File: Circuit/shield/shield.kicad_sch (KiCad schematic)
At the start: 6 parts, among them J1 Power, J2 Digital/PWM, J3 Analog, J4 Digital/PWM, J5 AE-TB6612, J6 Battery

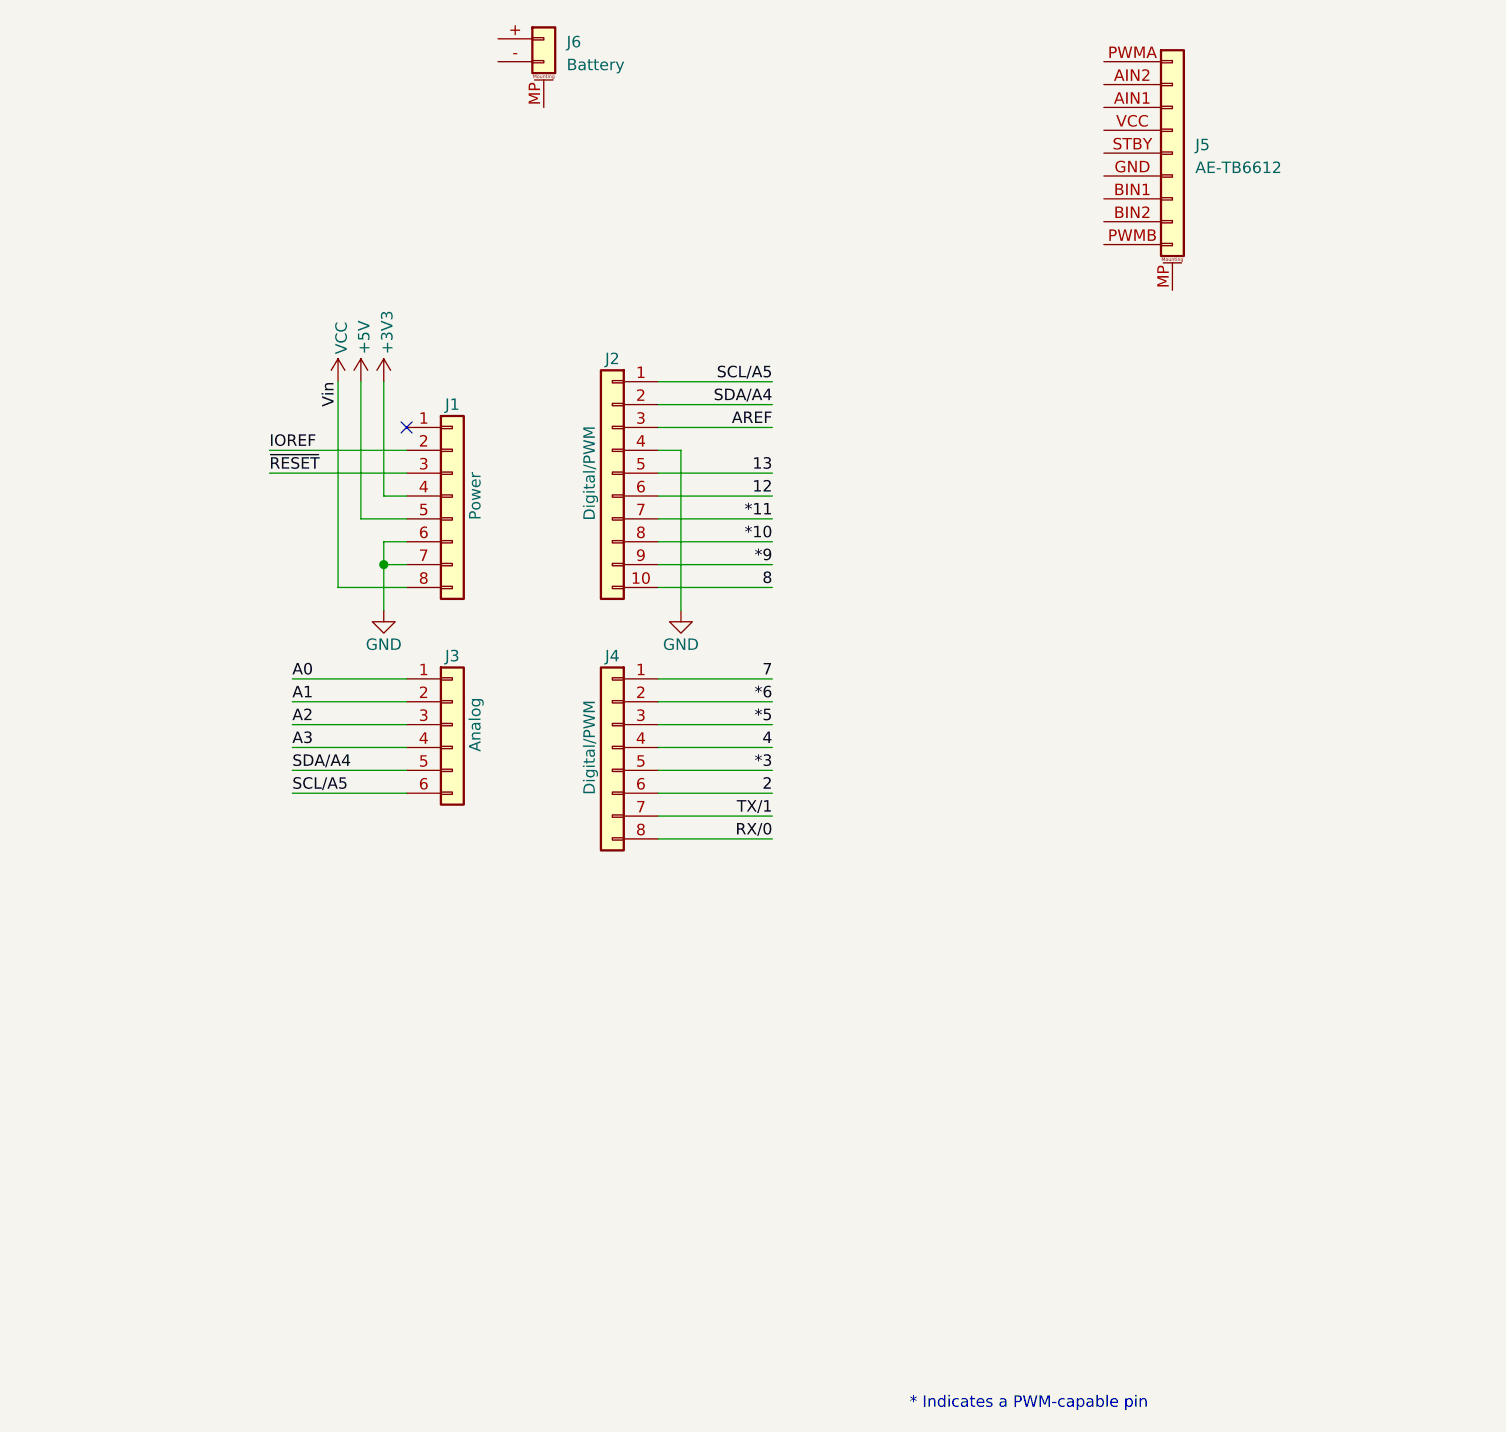
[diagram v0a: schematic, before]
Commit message: Make shield circuit
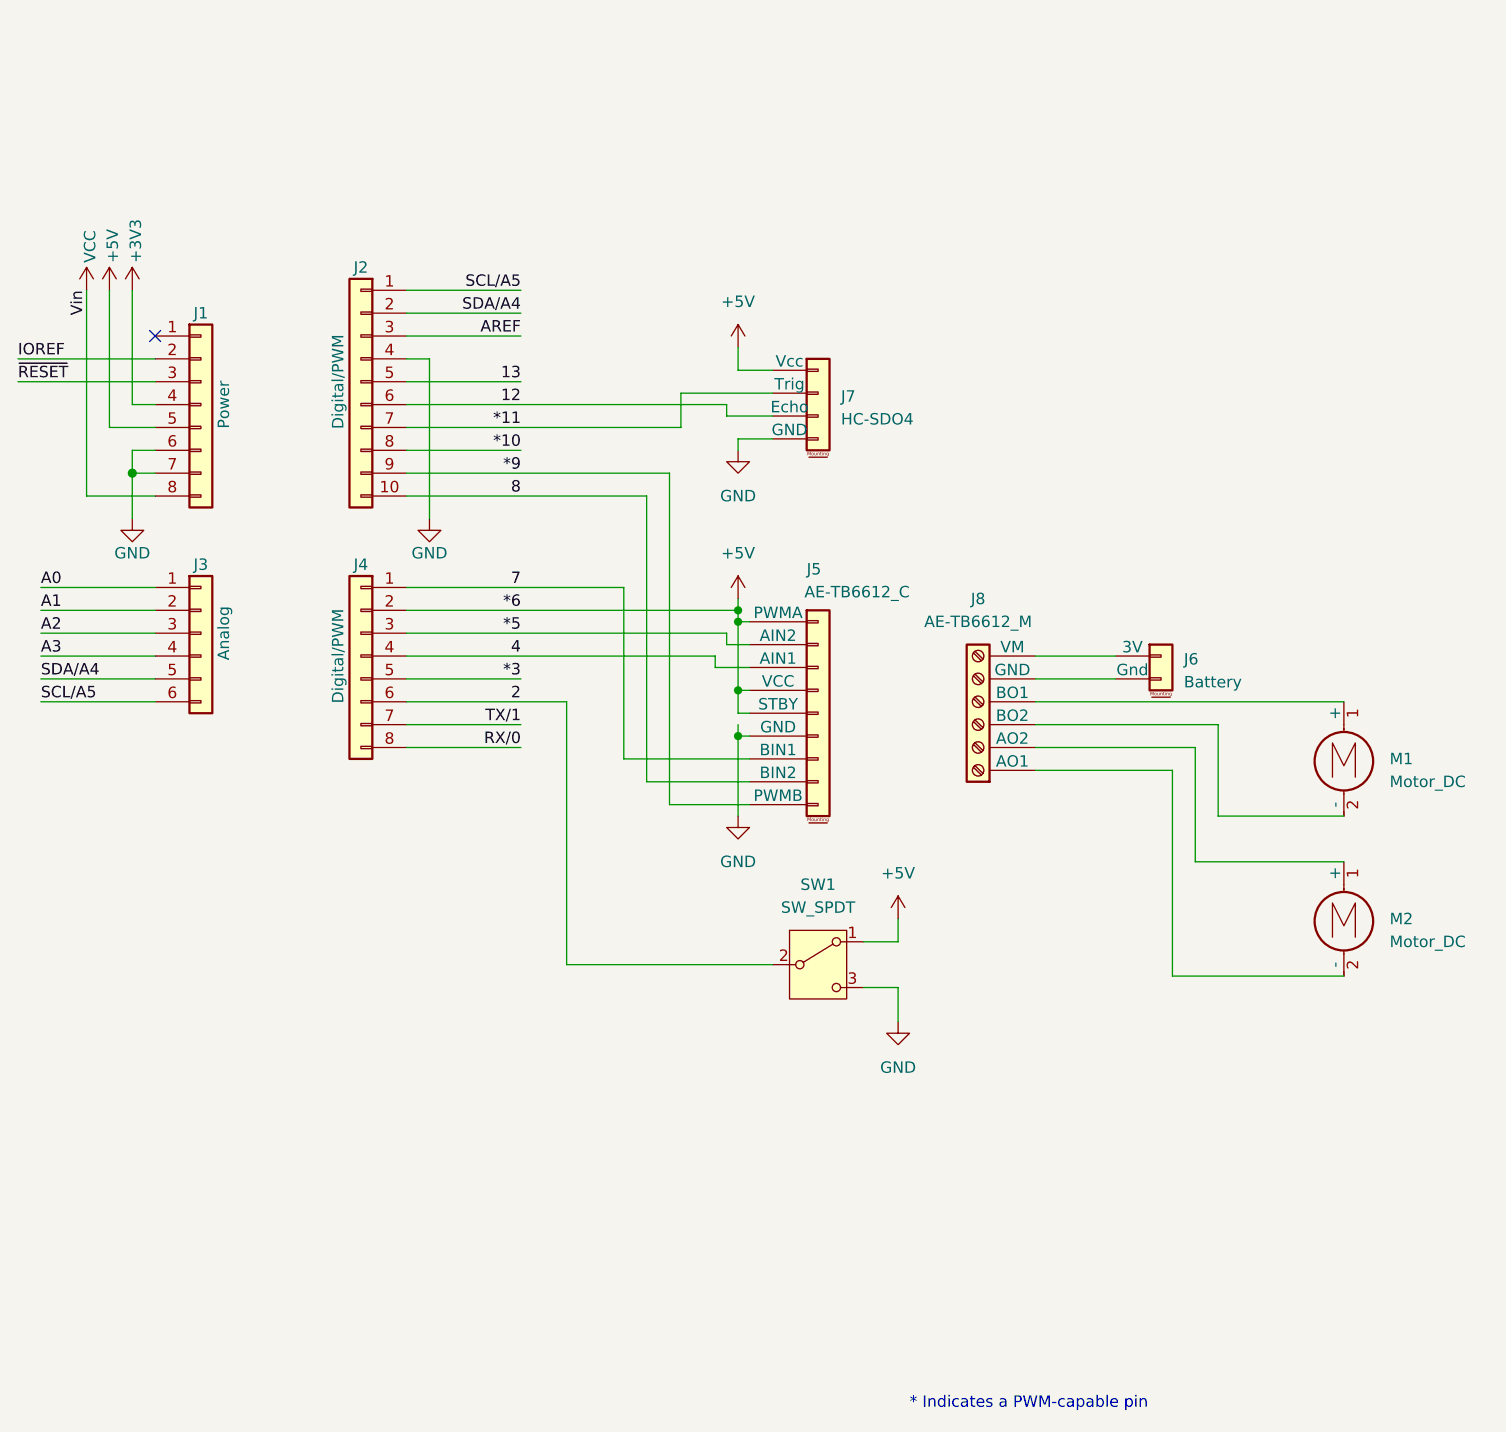
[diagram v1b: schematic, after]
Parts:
- added J8: AE-TB6612_M, symbol Connector:Screw_Terminal_01x06
- added M1, M2: Motor_DC, symbol Motor:Motor_DC
- added SW1: SW_SPDT, symbol Switch:SW_SPDT
- J5: value AE-TB6612 -> AE-TB6612_C
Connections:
- net *6 is gone; now on net +5V: J4.2 (Pin_2)
- net *5: now also J5.2 (AIN2)
- net *9: now also J5.9 (PWMB)
- net +5V: now also J5.1 (PWMA), J5.4 (VCC), J5.5 (STBY), SW1.1 (A)
- net 2: now also SW1.2 (B)
- net 4: now also J5.3 (AIN1)
- net 7: now also J5.7 (BIN1)
- net 8: now also J5.8 (BIN2)
- net GND: now also J5.6 (GND), SW1.3 (C)
- new net: J6.1 (3V), J8.6 (VM)
- new net: J6.2 (Gnd), J8.5 (GND)
- new net: J8.2 (AO2), M2.1 (+)
- new net: J8.1 (AO1), M2.2 (-)
- new net: J8.4 (BO1), M1.1 (+)
- new net: J8.3 (BO2), M1.2 (-)
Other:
- moved on the sheet: J1, J2, J3, J4

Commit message: 段階ごとにコードを分割
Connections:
- net +5V: no longer J4.2 (Pin_2), J5.1 (PWMA)
- new net *6: J4.2 (Pin_2), J5.1 (PWMA)
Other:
- moved on the sheet: J5
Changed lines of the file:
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@@
-	)
-	(junction
-		(at 158.75 91.44)
-		(diameter 0)
-		(color 0 0 0 0)
-	)
-	(junction
-		(at 158.75 92.71)
-		(diameter 0)
-		(color 0 0 0 0)
 	)
 	(junction
@@
 	)
 	(junction
-		(at 158.75 100.33)
+		(at 158.75 99.06)
 		(diameter 0)
 		(color 0 0 0 0)
 	)
-	(junction
-		(at 158.75 105.41)
-		(diameter 0)
-		(color 0 0 0 0)
-	)
 	(no_connect
 		(at 93.98 60.96)
@@
 	(wire
 		(pts
-			(xy 157.48 68.58) (xy 121.92 68.58)
+			(xy 121.92 68.58) (xy 162.56 68.58)
 		)
 		(stroke
@@
 	(wire
 		(pts
-			(xy 160.02 107.95) (xy 146.05 107.95)
+			(xy 160.02 106.68) (xy 146.05 106.68)
 		)
 		(stroke
@@
 	(wire
 		(pts
-			(xy 158.75 100.33) (xy 158.75 92.71)
-		)
-		(stroke
-			(width 0)
-			(type default)
-		)
-	)
-	(wire
-		(pts
 			(xy 88.9 55.88) (xy 88.9 71.12)
 		)
@@
 	(wire
 		(pts
-			(xy 160.02 102.87) (xy 158.75 102.87)
+			(xy 160.02 101.6) (xy 158.75 101.6)
 		)
 		(stroke
@@
 	(wire
 		(pts
-			(xy 160.02 113.03) (xy 151.13 113.03)
+			(xy 160.02 111.76) (xy 151.13 111.76)
 		)
 		(stroke
@@
 	(wire
 		(pts
-			(xy 157.48 69.85) (xy 162.56 69.85)
-		)
-		(stroke
-			(width 0)
-			(type solid)
-		)
-	)
-	(wire
-		(pts
-			(xy 152.4 67.31) (xy 152.4 71.12)
-		)
-		(stroke
-			(width 0)
-			(type default)
-		)
-	)
-	(wire
-		(pts
-			(xy 158.75 92.71) (xy 160.02 92.71)
-		)
-		(stroke
-			(width 0)
-			(type solid)
+			(xy 152.4 66.04) (xy 152.4 71.12)
+		)
+		(stroke
+			(width 0)
+			(type default)
 		)
 	)
@@
 	(wire
 		(pts
-			(xy 158.75 92.71) (xy 158.75 91.44)
-		)
-		(stroke
-			(width 0)
-			(type solid)
-		)
-	)
-	(wire
-		(pts
 			(xy 121.92 76.2) (xy 151.13 76.2)
 		)
@@
 	(wire
 		(pts
-			(xy 158.75 104.14) (xy 158.75 105.41)
+			(xy 158.75 104.14) (xy 158.75 114.3)
 		)
 		(stroke
@@
 	(wire
 		(pts
-			(xy 162.56 64.77) (xy 158.75 64.77)
-		)
-		(stroke
-			(width 0)
-			(type default)
-		)
-	)
-	(wire
-		(pts
-			(xy 156.21 97.79) (xy 160.02 97.79)
-		)
-		(stroke
-			(width 0)
-			(type solid)
-		)
-	)
-	(wire
-		(pts
-			(xy 158.75 102.87) (xy 158.75 100.33)
+			(xy 162.56 63.5) (xy 158.75 63.5)
 		)
 		(stroke
@@
 	(wire
 		(pts
-			(xy 146.05 107.95) (xy 146.05 88.9)
-		)
-		(stroke
-			(width 0)
-			(type default)
-		)
-	)
-	(wire
-		(pts
-			(xy 157.48 69.85) (xy 157.48 68.58)
-		)
-		(stroke
-			(width 0)
-			(type solid)
+			(xy 146.05 106.68) (xy 146.05 88.9)
+		)
+		(stroke
+			(width 0)
+			(type default)
 		)
 	)
@@
 	(wire
 		(pts
-			(xy 158.75 72.39) (xy 162.56 72.39)
-		)
-		(stroke
-			(width 0)
-			(type default)
-		)
-	)
-	(wire
-		(pts
-			(xy 158.75 105.41) (xy 160.02 105.41)
-		)
-		(stroke
-			(width 0)
-			(type default)
-		)
-	)
-	(wire
-		(pts
-			(xy 158.75 73.66) (xy 158.75 72.39)
+			(xy 158.75 71.12) (xy 162.56 71.12)
+		)
+		(stroke
+			(width 0)
+			(type default)
+		)
+	)
+	(wire
+		(pts
+			(xy 158.75 104.14) (xy 160.02 104.14)
+		)
+		(stroke
+			(width 0)
+			(type default)
+		)
+	)
+	(wire
+		(pts
+			(xy 158.75 73.66) (xy 158.75 71.12)
 		)
 		(stroke
@@
 	(wire
 		(pts
-			(xy 158.75 64.77) (xy 158.75 62.23)
+			(xy 158.75 63.5) (xy 158.75 62.23)
 		)
 		(stroke
@@
 	(wire
 		(pts
-			(xy 162.56 67.31) (xy 152.4 67.31)
-		)
-		(stroke
-			(width 0)
-			(type default)
-		)
-	)
-	(wire
-		(pts
-			(xy 156.21 96.52) (xy 121.92 96.52)
+			(xy 162.56 66.04) (xy 152.4 66.04)
+		)
+		(stroke
+			(width 0)
+			(type default)
+		)
+	)
+	(wire
+		(pts
+			(xy 121.92 96.52) (xy 160.02 96.52)
 		)
 		(stroke
@@
 	(wire
 		(pts
-			(xy 148.59 110.49) (xy 148.59 78.74)
+			(xy 148.59 109.22) (xy 148.59 78.74)
 		)
 		(stroke
@@
 	(wire
 		(pts
-			(xy 157.48 93.98) (xy 121.92 93.98)
-		)
-		(stroke
-			(width 0)
-			(type solid)
-		)
-	)
-	(wire
-		(pts
-			(xy 158.75 91.44) (xy 158.75 90.17)
+			(xy 121.92 93.98) (xy 160.02 93.98)
+		)
+		(stroke
+			(width 0)
+			(type solid)
+		)
+	)
+	(wire
+		(pts
+			(xy 158.75 90.17) (xy 158.75 101.6)
 		)
 		(stroke
@@
 	(wire
 		(pts
-			(xy 151.13 113.03) (xy 151.13 76.2)
-		)
-		(stroke
-			(width 0)
-			(type default)
-		)
-	)
-	(wire
-		(pts
-			(xy 158.75 100.33) (xy 160.02 100.33)
-		)
-		(stroke
-			(width 0)
-			(type default)
-		)
-	)
-	(wire
-		(pts
-			(xy 157.48 95.25) (xy 160.02 95.25)
-		)
-		(stroke
-			(width 0)
-			(type solid)
+			(xy 151.13 111.76) (xy 151.13 76.2)
+		)
+		(stroke
+			(width 0)
+			(type default)
+		)
+	)
+	(wire
+		(pts
+			(xy 158.75 99.06) (xy 160.02 99.06)
+		)
+		(stroke
+			(width 0)
+			(type default)
 		)
 	)
@@
 	(wire
 		(pts
-			(xy 160.02 110.49) (xy 148.59 110.49)
+			(xy 160.02 109.22) (xy 148.59 109.22)
 		)
 		(stroke
@@
 	(wire
 		(pts
-			(xy 158.75 105.41) (xy 158.75 114.3)
-		)
-		(stroke
-			(width 0)
-			(type default)
-		)
-	)
-	(wire
-		(pts
 			(xy 121.92 99.06) (xy 134.62 99.06)
 		)
@@
 	(wire
 		(pts
-			(xy 158.75 91.44) (xy 121.92 91.44)
+			(xy 121.92 91.44) (xy 160.02 91.44)
 		)
 		(stroke
@@
 		(pts
 			(xy 121.92 78.74) (xy 148.59 78.74)
-		)
-		(stroke
-			(width 0)
-			(type solid)
-		)
-	)
-	(wire
-		(pts
-			(xy 157.48 95.25) (xy 157.48 93.98)
-		)
-		(stroke
-			(width 0)
-			(type solid)
-		)
-	)
-	(wire
-		(pts
-			(xy 156.21 97.79) (xy 156.21 96.52)
 		)
 		(stroke
@@
 	(symbol
 		(lib_id "Connector_Generic_MountingPin:Conn_01x04_MountingPin")
-		(at 167.64 67.31 0)
+		(at 167.64 66.04 0)
 		(unit 1)
 		(body_style 1)
@@
 		(fields_autoplaced yes)
 		(property "Reference" "J7"
-			(at 170.18 67.6655 0)
+			(at 170.18 66.3955 0)
 			(show_name no)
 			(do_not_autoplace no)
@@
 		)
 		(property "Value" "HC-SDO4"
-			(at 170.18 70.2055 0)
+			(at 170.18 68.9355 0)
 			(show_name no)
 			(do_not_autoplace no)
@@
 		)
 		(property "Footprint" ""
-			(at 167.64 67.31 0)
+			(at 167.64 66.04 0)
 			(hide yes)
 			(show_name no)
@@
 		)
 		(property "Datasheet" ""
-			(at 167.64 67.31 0)
+			(at 167.64 66.04 0)
 			(hide yes)
 			(show_name no)
@@
 		)
 		(property "Description" "Generic connectable mounting pin connector, single row, 01x04, script generated (kicad-library-utils/schlib/autogen/connector/)"
-			(at 167.64 67.31 0)
+			(at 167.64 66.04 0)
 			(hide yes)
 			(show_name no)
@@
 	(symbol
 		(lib_id "Connector_Generic_MountingPin:Conn_01x09_MountingPin")
-		(at 167.64 102.87 0)
+		(at 167.64 101.6 0)
 		(unit 1)
 		(body_style 1)
@@
 		(dnp no)
 		(property "Reference" "J5"
-			(at 166.37 86.868 0)
+			(at 166.37 85.598 0)
 			(show_name no)
 			(do_not_autoplace no)
@@
 		)
 		(property "Value" "AE-TB6612_C"
-			(at 166.116 89.408 0)
+			(at 166.116 88.138 0)
 			(show_name no)
 			(do_not_autoplace no)
@@
 		)
 		(property "Footprint" ""
-			(at 167.64 102.87 0)
+			(at 167.64 101.6 0)
 			(hide yes)
 			(show_name no)
@@
 		)
 		(property "Datasheet" ""
-			(at 167.64 102.87 0)
+			(at 167.64 101.6 0)
 			(hide yes)
 			(show_name no)
@@
 		)
 		(property "Description" "Generic connectable mounting pin connector, single row, 01x09, script generated (kicad-library-utils/schlib/autogen/connector/)"
-			(at 167.64 102.87 0)
-			(hide yes)
-			(show_name no)
+			(at 167.64 101.6 0)
+			(hide yes)
+			(show_name no)
